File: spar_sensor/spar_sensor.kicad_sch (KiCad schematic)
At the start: 24 parts, among them J1 Conn_01x03_Pin, J2 Conn_01x04_Pin, J3 Conn_01x04_Pin, J4 AVR-ISP-6, Q1 MMSS8550, Q2 2N7002K, SW1 SW_DPST_x2, U1 HX711, U2 ATtiny85-20M

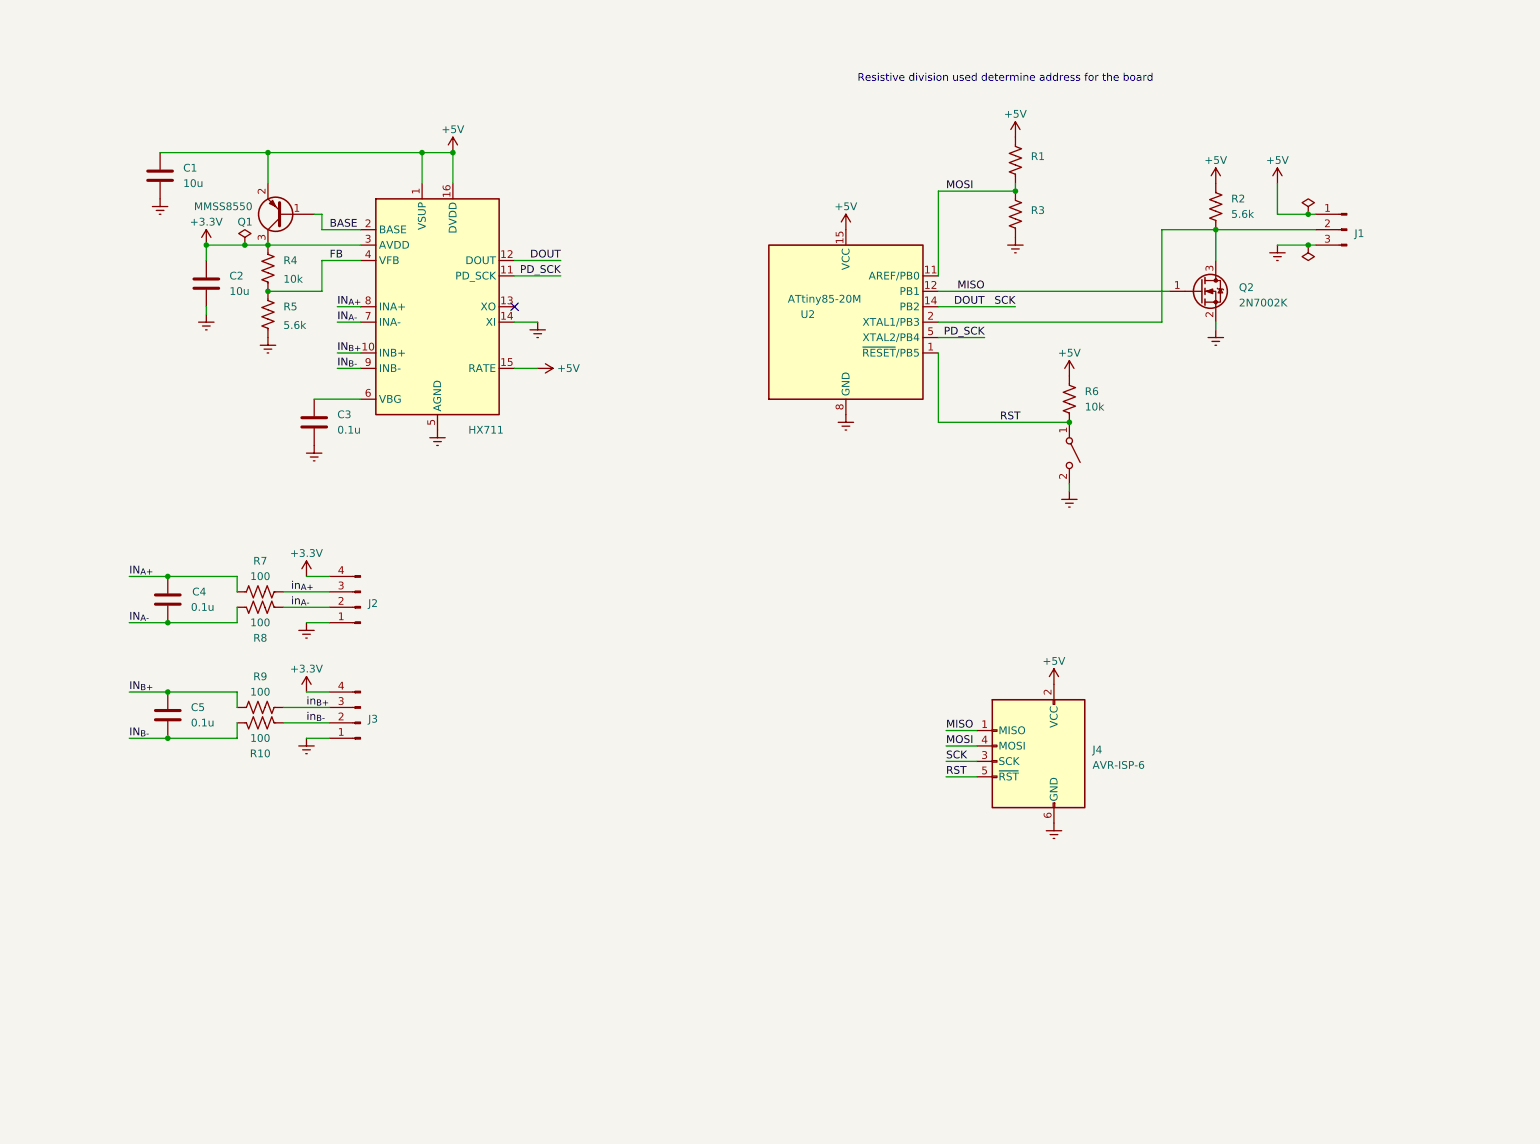
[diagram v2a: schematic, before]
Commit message: Completed spar sensor revised schematic
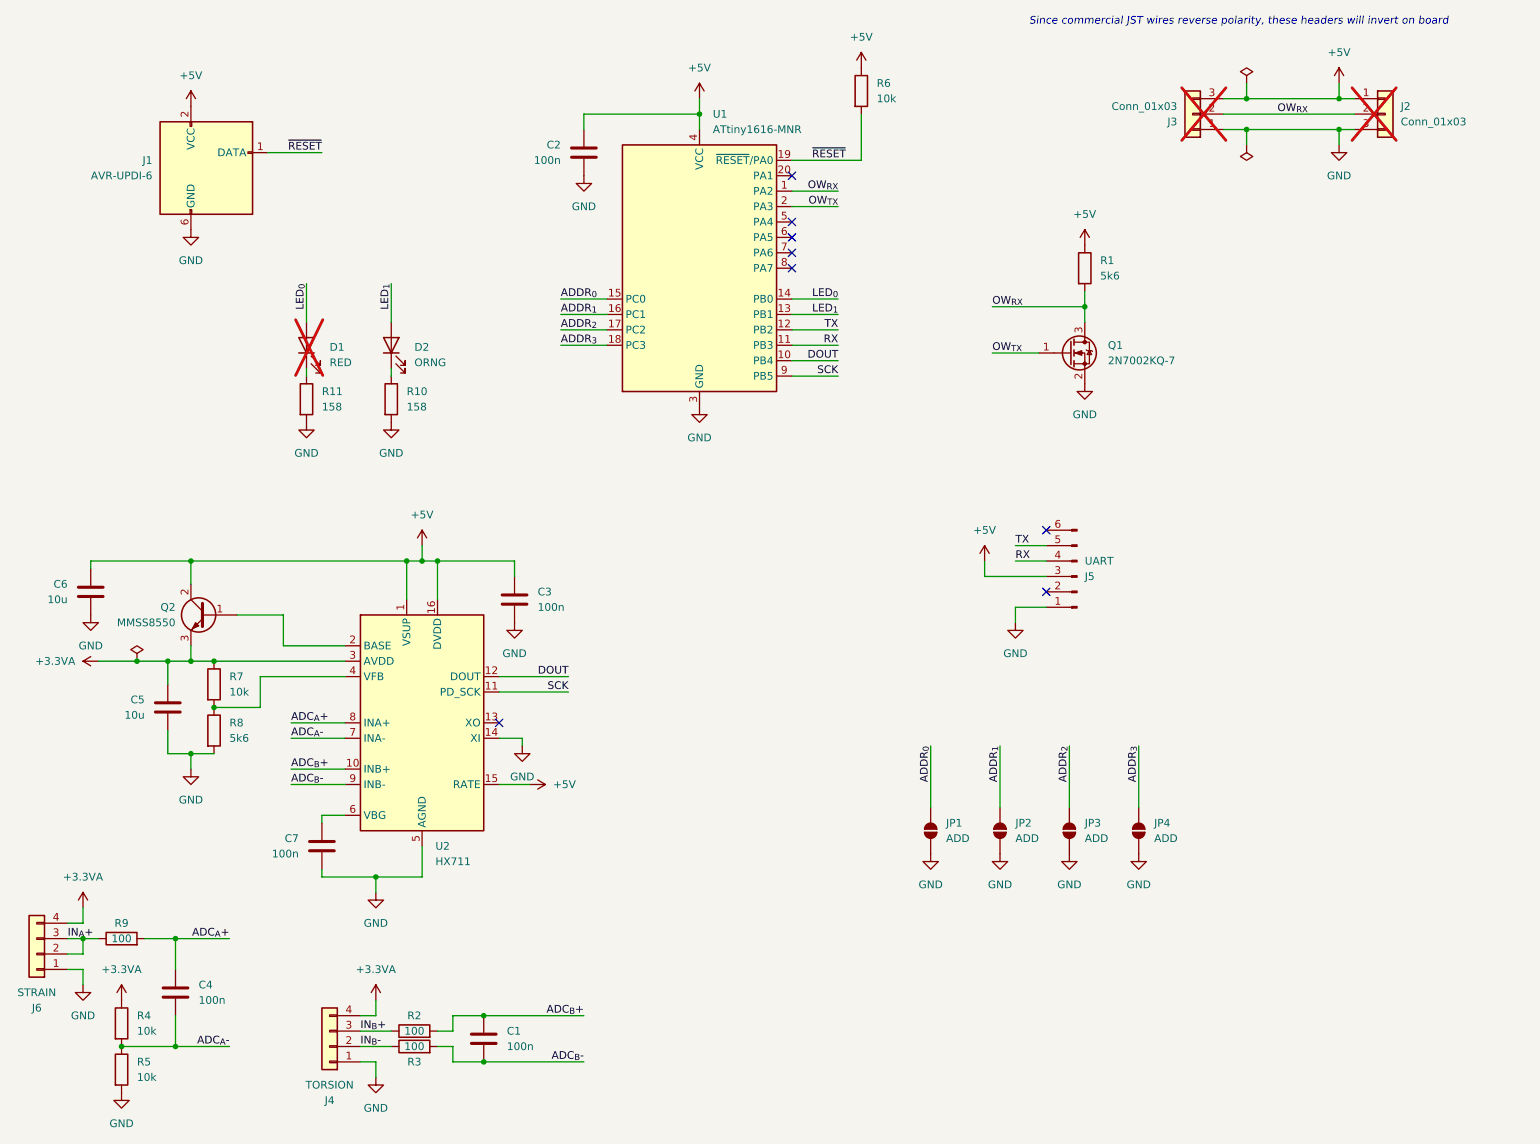
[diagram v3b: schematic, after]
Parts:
- removed J1: Conn_01x03_Pin, Connector_JST:JST_EH_B3B-EH-A_1x03_P2.50mm_Vertical, symbol Connector:Conn_01x03_Pin
- removed J2, J3: Conn_01x04_Pin, Connector_PinHeader_2.54mm:PinHeader_1x04_P2.54mm_Vertical, symbol Connector:Conn_01x04_Pin
- removed J4: AVR-ISP-6, Connector_PinHeader_2.54mm:PinHeader_2x03_P2.54mm_Vertical_SMD, symbol Connector:AVR-ISP-6
- removed Q1: MMSS8550, Package_TO_SOT_SMD:SOT-23, symbol Device:Q_PNP_BEC
- removed Q2: 2N7002K, Package_TO_SOT_SMD:SOT-23, symbol Transistor_FET:2N7002K
- removed R1, R3: R_US, Resistor_SMD:R_0603_1608Metric, symbol Device:R_US
- removed R10, R7, R8, R9: 100, Resistor_SMD:R_0603_1608Metric, symbol Device:R_US
- removed R2, R5: 5.6k, Resistor_SMD:R_0603_1608Metric, symbol Device:R_US
- removed R4, R6: 10k, Resistor_SMD:R_0603_1608Metric, symbol Device:R_US
- removed SW1: SW_DPST_x2, Button_Switch_SMD:SW_SPST_SKQG_WithStem, symbol Switch:SW_SPST
- removed U1: HX711, Package_SO:SOP-16_3.9x9.9mm_P1.27mm, symbol Analog_ADC:HX711
- removed U2: ATtiny85-20M, Package_DFN_QFN:QFN-20-1EP_4x4mm_P0.5mm_EP2.6x2.6mm, symbol MCU_Microchip_ATtiny:ATtiny85-20M
- added C6: 10u, Capacitor_SMD:C_0603_1608Metric, symbol Device:C
- added C7: 100n, Capacitor_SMD:C_0402_1005Metric, symbol Device:C
- added D1: RED, LED_SMD:LED_0805_2012Metric, symbol Device:LED
- added D2: ORNG, LED_SMD:LED_0805_2012Metric, symbol Device:LED
- added J1: AVR-UPDI-6, Connector:Tag-Connect_TC2030-IDC-NL_2x03_P1.27mm_Vertical, symbol Connector:AVR-UPDI-6
- added J2, J3: Conn_01x03, Connector_JST:JST_EH_B3B-EH-A_1x03_P2.50mm_Vertical, symbol Connector_Generic:Conn_01x03
- added J4: TORSION, Connector_PinHeader_2.00mm:PinHeader_1x04_P2.00mm_Vertical, symbol Connector_Generic:Conn_01x04
- added J5: UART, Connector_PinHeader_2.54mm:PinHeader_1x06_P2.54mm_Vertical, symbol Connector:Conn_01x06_Pin
- added J6: STRAIN, Connector_PinHeader_2.00mm:PinHeader_1x04_P2.00mm_Vertical, symbol Connector_Generic:Conn_01x04
- added JP1, JP2, JP3, JP4: ADD, Jumper:SolderJumper-2_P1.3mm_Open_TrianglePad1.0x1.5mm, symbol Jumper:SolderJumper_2_Open
- added Q1: 2N7002KQ-7, Package_TO_SOT_SMD:SOT-23, symbol Transistor_FET:2N7002
- added Q2: MMSS8550, Package_TO_SOT_SMD:SOT-23, symbol Device:Q_NPN_BCE
- added R1, R8: 5k6, Resistor_SMD:R_0402_1005Metric, symbol Device:R
- added R10, R11: 158, Resistor_SMD:R_0603_1608Metric, symbol Device:R
- added R2, R3, R9: 100, Resistor_SMD:R_0402_1005Metric, symbol Device:R
- added R4, R5, R6, R7: 10k, Resistor_SMD:R_0402_1005Metric, symbol Device:R
- added U1: ATtiny1616-MNR, Package_DFN_QFN:VQFN-20-1EP_3x3mm_P0.4mm_EP1.7x1.7mm, symbol MCU_Microchip_ATtiny:ATtiny1616-M
- added U2: HX711, Package_SO:SOP-16_3.9x9.9mm_P1.27mm, symbol Analog_ADC:HX711
- C1, C2: value 10u -> 100n; footprint Capacitor_SMD:C_0603_1608Metric -> Capacitor_SMD:C_0402_1005Metric; LCSC (none) -> C5448875
- C3, C4: value 0.1u -> 100n; footprint Capacitor_SMD:C_0603_1608Metric -> Capacitor_SMD:C_0402_1005Metric; LCSC (none) -> C5448875
- C5: value 0.1u -> 10u; LCSC (none) -> C5360828
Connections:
- net +3.3V is gone; now on net +5V: C2.1
- net IN_{B+} is gone; now on net GND: C5.2
- net +5V: now also C3.1, C6.1, J1.2 (VCC), J2.1 (Pin_1), J3.3 (Pin_3), J5.3 (Pin_3), Q2.2 (C), R1.1, R6.1, U1.4 (VCC), U2.1 (VSUP), U2.15 (RATE), U2.16 (DVDD); no longer C1.1
- net DOUT: now also U1.10 (PB4), U2.12 (DOUT)
- net GND: now reaches C3.2
- net GND: now also C2.2, C6.2, C7.2, J1.6 (GND), J2.3 (Pin_3), J3.1 (Pin_1), J4.1 (Pin_1), J5.1 (Pin_1), J6.1 (Pin_1), JP1.1 (A), JP2.1 (A), JP3.1 (A), JP4.1 (A), Q1.2 (S), R10.2, R11.2, R5.2, R8.2, U1.21 (GND), U1.3 (GND), U2.14 (XI), U2.5 (AGND)
- removed net GNDREF: C1.2, C2.2, C3.1
- net IN_{A+} renamed ADC_{A}-
- net ADC_{A}-: now also R4.2, R5.1, U2.7 (INA-)
- net IN_{A-} renamed ADC_{A}+
- net ADC_{A}+: now also R9.2, U2.8 (INA+)
- net IN_{B-} renamed +3.3VA
- net +3.3VA: now also J4.4 (Pin_4), J6.4 (Pin_4), Q2.3 (E), R4.1, R7.1, U2.3 (AVDD)
- new net: R7.2, R8.1, U2.4 (VFB)
- new net: D1.1 (K), R11.1
- new net: Q2.1 (B), U2.2 (BASE)
- new net: D2.1 (K), R10.1
- new net: C7.1, U2.6 (VBG)
- new net ADC_{B}+: C1.1, R2.2, U2.10 (INB+)
- new net ADC_{B}-: C1.2, R3.2, U2.9 (INB-)
- new net ADDR_{0}: JP1.2 (B), U1.15 (PC0)
- new net ADDR_{1}: JP2.2 (B), U1.16 (PC1)
- new net ADDR_{2}: JP3.2 (B), U1.17 (PC2)
- new net ADDR_{3}: JP4.2 (B), U1.18 (PC3)
- new net IN_{A}+: J6.2 (Pin_2), J6.3 (Pin_3), R9.1
- new net IN_{B}+: J4.3 (Pin_3), R2.1
- new net IN_{B}-: J4.2 (Pin_2), R3.1
- new net LED_{0}: D1.2 (A), U1.14 (PB0)
- new net LED_{1}: D2.2 (A), U1.13 (PB1)
- new net OW_{RX}: J2.2 (Pin_2), J3.2 (Pin_2), Q1.3 (D), R1.2, U1.1 (PA2)
- new net OW_{TX}: Q1.1 (G), U1.2 (PA3)
- new net RX: J5.4 (Pin_4), U1.11 (PB3)
- new net SCK: U1.9 (PB5), U2.11 (PD_SCK)
- new net TX: J5.5 (Pin_5), U1.12 (PB2)
- new net ~{RESET}: J1.1 (DATA), R6.2, U1.19 (~{RESET}/PA0)
- no-connect marks 1 -> 8
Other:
- note added: "Since commercial JST wires reverse polarity, these headers will invert on board"
- note removed: "Resistive division used determine address for the board"

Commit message: Completed PCB layout of ATtiny1616 based strain gauge board
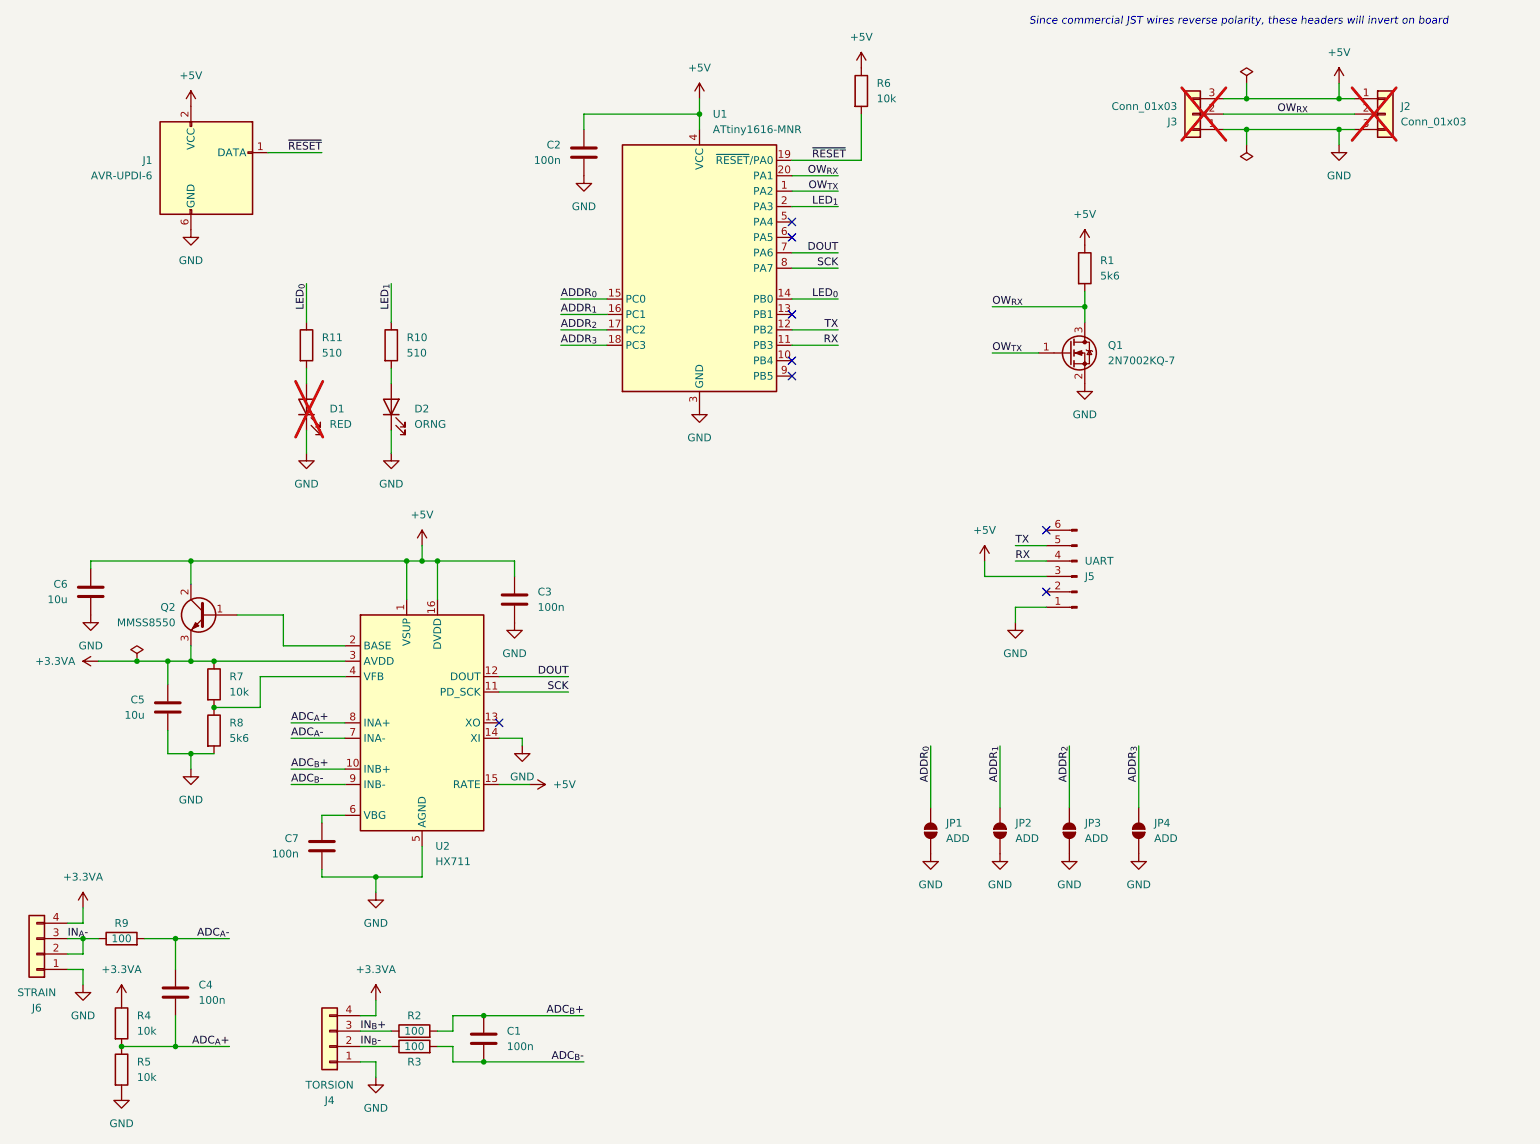
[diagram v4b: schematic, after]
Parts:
- J1: now left out of the parts list
- R10, R11: value 158 -> 510; footprint Resistor_SMD:R_0603_1608Metric -> Resistor_SMD:R_0402_1005Metric; LCSC C22884 -> C2991609
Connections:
- net ADC_{A}+: now also C4.2, R4.2, R5.1; no longer C4.1, R9.2
- net ADC_{A}-: now also C4.1, R9.2; no longer C4.2, R4.2, R5.1
- net DOUT: now also U1.7 (PA6); no longer U1.10 (PB4)
- net GND: now also D1.1 (K), D2.1 (K); no longer R10.2, R11.2
- net LED_{0}: now also R11.1; no longer D1.2 (A)
- net LED_{1}: now also R10.1, U1.2 (PA3); no longer D2.2 (A), U1.13 (PB1)
- net OW_{RX}: now also U1.20 (PA1); no longer U1.1 (PA2)
- net OW_{TX}: now also U1.1 (PA2); no longer U1.2 (PA3)
- net SCK: now also U1.8 (PA7); no longer U1.9 (PB5)
- net IN_{A}+ renamed IN_{A}-
- new net: D2.2 (A), R10.2
- new net: D1.2 (A), R11.2
